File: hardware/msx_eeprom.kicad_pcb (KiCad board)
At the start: 2 copper layers, 102.8 x 65.4 mm, 102 parts, among them J1 Conn_02x07_Odd_Even, P1 MSX_CONNECTOR, U1 AT28C256-15PU

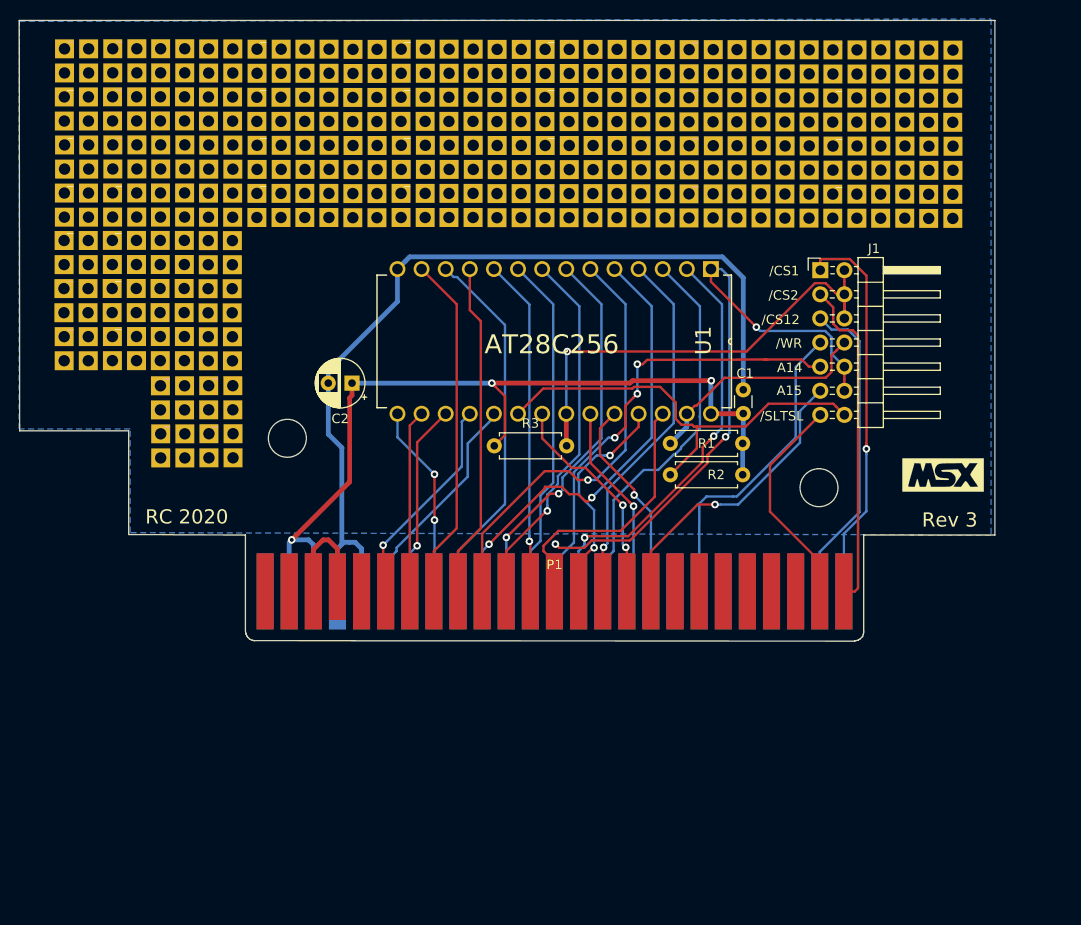
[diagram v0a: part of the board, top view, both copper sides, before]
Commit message: Moved PCB mounting hole up by 1mm
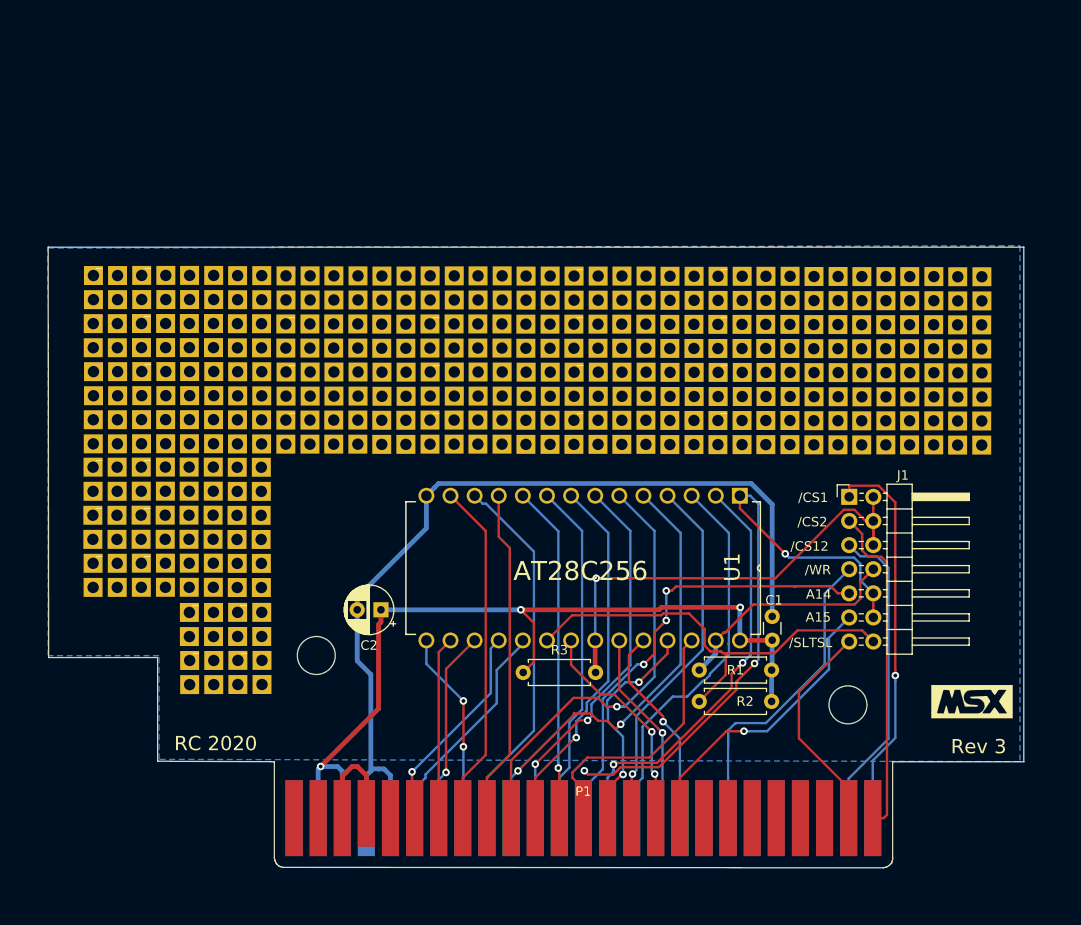
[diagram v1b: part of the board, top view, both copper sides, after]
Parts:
- removed the _ at (96.9, 67.8)
- removed the _ at (96.9, 57.6)
- removed the _ at (86.8, 57.6)
- removed the _ at (96.9, 52.5)
- removed the _ at (91.9, 62.7)
- removed the _ at (102.0, 62.7)
- removed the _ at (96.9, 62.7)
- removed the _ at (86.8, 62.7)
- removed the _ at (117.2, 32.4)
- removed the _ at (157.6, 32.4)
- removed the _ at (127.3, 32.4)
- removed the _ at (102.0, 67.8)
- removed the _ at (172.8, 32.5)
- removed the _ at (132.4, 32.4)
- removed the _ at (107.1, 32.4)
- removed the _ at (122.3, 32.4)
- removed the _ at (91.9, 32.3)
- removed the _ at (167.7, 32.5)
- removed the _ at (102.0, 32.4)
- removed the _ at (112.1, 32.4)
- removed the _ at (142.5, 32.4)
- removed the _ at (177.9, 32.5)
- removed the _ at (102.0, 72.9)
- removed the _ at (162.7, 32.5)
- removed the _ at (137.4, 32.4)
- removed the _ at (147.5, 32.4)
- removed the _ at (96.9, 32.3)
- removed the _ at (122.3, 37.5)
- removed the _ at (86.8, 32.4)
- removed the _ at (152.6, 32.4)
- removed the _ at (132.4, 37.5)
- removed the _ at (127.3, 37.5)
- removed the _ at (172.8, 37.5)
- removed the _ at (96.9, 72.9)
- removed the _ at (91.9, 37.4)
- removed the _ at (102.0, 37.4)
- removed the _ at (112.1, 37.5)
- removed the _ at (107.1, 37.5)
- removed the _ at (117.2, 37.5)
- removed the _ at (167.7, 37.5)
- removed the _ at (177.8, 37.6)
- removed the _ at (142.5, 37.5)
- removed the _ at (157.6, 37.5)
- removed the _ at (152.6, 37.5)
- removed the _ at (91.9, 52.5)
- removed the _ at (162.7, 37.5)
- removed the _ at (137.4, 37.5)
- removed the _ at (147.5, 37.5)
- removed the _ at (86.8, 37.4)
- removed the _ at (96.9, 37.4)
- removed the _ at (122.3, 42.5)
- removed the _ at (132.4, 42.5)
- removed the _ at (127.3, 42.5)
- removed the _ at (172.8, 42.6)
- removed the _ at (91.9, 42.5)
- removed the _ at (102.0, 52.6)
- removed the _ at (102.0, 42.5)
- removed the _ at (112.1, 42.5)
- removed the _ at (107.1, 42.5)
- removed the _ at (117.2, 42.5)
- removed the _ at (167.8, 42.6)
- removed the _ at (177.9, 42.6)
- removed the _ at (142.5, 42.5)
- removed the _ at (157.7, 42.6)
- removed the _ at (152.6, 42.6)
- removed the _ at (162.7, 42.6)
- removed the _ at (101.9, 57.6)
- removed the _ at (137.4, 42.5)
- removed the _ at (147.5, 42.6)
- removed the _ at (86.8, 42.5)
- removed the _ at (96.9, 42.5)
- removed the _ at (86.8, 47.5)
- removed the _ at (96.9, 47.5)
- removed the _ at (91.9, 47.5)
- removed the _ at (102.0, 47.6)
- removed the _ at (112.1, 47.6)
- removed the _ at (107.1, 47.6)
- removed the _ at (91.8, 57.6)
- removed the _ at (117.2, 47.6)
- removed the _ at (172.8, 47.7)
- removed the _ at (167.7, 47.7)
- removed the _ at (177.8, 47.7)
- removed the _ at (157.6, 47.6)
- removed the _ at (152.6, 47.6)
- removed the _ at (162.7, 47.6)
- removed the _ at (137.4, 47.6)
- removed the _ at (147.5, 47.6)
- removed the _ at (142.5, 47.6)
- removed the _ at (86.8, 52.5)
- removed the _ at (132.4, 47.6)
- removed the _ at (127.3, 47.6)
- removed the _ at (122.3, 47.6)
- added _: _, Connector_Wire:SolderWirePad_2x02_P2.54mm_Drill0.8mm, F.Cu at (100.0, 91.7)
- added _: _, Connector_Wire:SolderWirePad_2x02_P2.54mm_Drill0.8mm, F.Cu at (99.9, 81.5)
- added _: _, Connector_Wire:SolderWirePad_2x02_P2.54mm_Drill0.8mm, F.Cu at (89.8, 81.5)
- added _: _, Connector_Wire:SolderWirePad_2x02_P2.54mm_Drill0.8mm, F.Cu at (99.9, 76.4)
- added _: _, Connector_Wire:SolderWirePad_2x02_P2.54mm_Drill0.8mm, F.Cu at (94.9, 86.5)
- added _: _, Connector_Wire:SolderWirePad_2x02_P2.54mm_Drill0.8mm, F.Cu at (105.0, 86.6)
- added _: _, Connector_Wire:SolderWirePad_2x02_P2.54mm_Drill0.8mm, F.Cu at (99.9, 86.5)
- added _: _, Connector_Wire:SolderWirePad_2x02_P2.54mm_Drill0.8mm, F.Cu at (89.8, 86.5)
- added _: _, Connector_Wire:SolderWirePad_2x02_P2.54mm_Drill0.8mm, F.Cu at (120.2, 56.3)
- added _: _, Connector_Wire:SolderWirePad_2x02_P2.54mm_Drill0.8mm, F.Cu at (160.7, 56.3)
- added _: _, Connector_Wire:SolderWirePad_2x02_P2.54mm_Drill0.8mm, F.Cu at (130.4, 56.3)
- added _: _, Connector_Wire:SolderWirePad_2x02_P2.54mm_Drill0.8mm, F.Cu at (105.0, 91.7)
- added _: _, Connector_Wire:SolderWirePad_2x02_P2.54mm_Drill0.8mm, F.Cu at (175.8, 56.3)
- added _: _, Connector_Wire:SolderWirePad_2x02_P2.54mm_Drill0.8mm, F.Cu at (135.4, 56.3)
- added _: _, Connector_Wire:SolderWirePad_2x02_P2.54mm_Drill0.8mm, F.Cu at (110.1, 56.3)
- added _: _, Connector_Wire:SolderWirePad_2x02_P2.54mm_Drill0.8mm, F.Cu at (125.3, 56.3)
- added _: _, Connector_Wire:SolderWirePad_2x02_P2.54mm_Drill0.8mm, F.Cu at (94.9, 56.2)
- added _: _, Connector_Wire:SolderWirePad_2x02_P2.54mm_Drill0.8mm, F.Cu at (170.8, 56.3)
- added _: _, Connector_Wire:SolderWirePad_2x02_P2.54mm_Drill0.8mm, F.Cu at (105.0, 56.2)
- added _: _, Connector_Wire:SolderWirePad_2x02_P2.54mm_Drill0.8mm, F.Cu at (115.2, 56.3)
- added _: _, Connector_Wire:SolderWirePad_2x02_P2.54mm_Drill0.8mm, F.Cu at (145.5, 56.3)
- added _: _, Connector_Wire:SolderWirePad_2x02_P2.54mm_Drill0.8mm, F.Cu at (180.9, 56.4)
- added _: _, Connector_Wire:SolderWirePad_2x02_P2.54mm_Drill0.8mm, F.Cu at (105.1, 96.8)
- added _: _, Connector_Wire:SolderWirePad_2x02_P2.54mm_Drill0.8mm, F.Cu at (165.8, 56.3)
- added _: _, Connector_Wire:SolderWirePad_2x02_P2.54mm_Drill0.8mm, F.Cu at (140.5, 56.3)
- added _: _, Connector_Wire:SolderWirePad_2x02_P2.54mm_Drill0.8mm, F.Cu at (150.6, 56.3)
- added _: _, Connector_Wire:SolderWirePad_2x02_P2.54mm_Drill0.8mm, F.Cu at (100.0, 56.2)
- added _: _, Connector_Wire:SolderWirePad_2x02_P2.54mm_Drill0.8mm, F.Cu at (125.3, 61.3)
- added _: _, Connector_Wire:SolderWirePad_2x02_P2.54mm_Drill0.8mm, F.Cu at (89.9, 56.2)
- added _: _, Connector_Wire:SolderWirePad_2x02_P2.54mm_Drill0.8mm, F.Cu at (155.7, 56.3)
- added _: _, Connector_Wire:SolderWirePad_2x02_P2.54mm_Drill0.8mm, F.Cu at (135.4, 61.4)
- added _: _, Connector_Wire:SolderWirePad_2x02_P2.54mm_Drill0.8mm, F.Cu at (130.3, 61.3)
- added _: _, Connector_Wire:SolderWirePad_2x02_P2.54mm_Drill0.8mm, F.Cu at (175.8, 61.4)
- added _: _, Connector_Wire:SolderWirePad_2x02_P2.54mm_Drill0.8mm, F.Cu at (100.0, 96.8)
- added _: _, Connector_Wire:SolderWirePad_2x02_P2.54mm_Drill0.8mm, F.Cu at (94.9, 61.3)
- added _: _, Connector_Wire:SolderWirePad_2x02_P2.54mm_Drill0.8mm, F.Cu at (105.0, 61.3)
- added _: _, Connector_Wire:SolderWirePad_2x02_P2.54mm_Drill0.8mm, F.Cu at (115.2, 61.3)
- added _: _, Connector_Wire:SolderWirePad_2x02_P2.54mm_Drill0.8mm, F.Cu at (110.1, 61.3)
- added _: _, Connector_Wire:SolderWirePad_2x02_P2.54mm_Drill0.8mm, F.Cu at (120.2, 61.4)
- added _: _, Connector_Wire:SolderWirePad_2x02_P2.54mm_Drill0.8mm, F.Cu at (170.8, 61.4)
- added _: _, Connector_Wire:SolderWirePad_2x02_P2.54mm_Drill0.8mm, F.Cu at (180.9, 61.4)
- added _: _, Connector_Wire:SolderWirePad_2x02_P2.54mm_Drill0.8mm, F.Cu at (145.5, 61.4)
- added _: _, Connector_Wire:SolderWirePad_2x02_P2.54mm_Drill0.8mm, F.Cu at (160.7, 61.4)
- added _: _, Connector_Wire:SolderWirePad_2x02_P2.54mm_Drill0.8mm, F.Cu at (155.6, 61.4)
- added _: _, Connector_Wire:SolderWirePad_2x02_P2.54mm_Drill0.8mm, F.Cu at (94.9, 76.4)
- added _: _, Connector_Wire:SolderWirePad_2x02_P2.54mm_Drill0.8mm, F.Cu at (165.7, 61.4)
- added _: _, Connector_Wire:SolderWirePad_2x02_P2.54mm_Drill0.8mm, F.Cu at (140.5, 61.4)
- added _: _, Connector_Wire:SolderWirePad_2x02_P2.54mm_Drill0.8mm, F.Cu at (150.6, 61.4)
- added _: _, Connector_Wire:SolderWirePad_2x02_P2.54mm_Drill0.8mm, F.Cu at (89.8, 61.3)
- added _: _, Connector_Wire:SolderWirePad_2x02_P2.54mm_Drill0.8mm, F.Cu at (100.0, 61.3)
- added _: _, Connector_Wire:SolderWirePad_2x02_P2.54mm_Drill0.8mm, F.Cu at (125.3, 66.4)
- added _: _, Connector_Wire:SolderWirePad_2x02_P2.54mm_Drill0.8mm, F.Cu at (135.4, 66.4)
- added _: _, Connector_Wire:SolderWirePad_2x02_P2.54mm_Drill0.8mm, F.Cu at (130.4, 66.4)
- added _: _, Connector_Wire:SolderWirePad_2x02_P2.54mm_Drill0.8mm, F.Cu at (175.8, 66.5)
- added _: _, Connector_Wire:SolderWirePad_2x02_P2.54mm_Drill0.8mm, F.Cu at (94.9, 66.3)
- added _: _, Connector_Wire:SolderWirePad_2x02_P2.54mm_Drill0.8mm, F.Cu at (105.0, 76.4)
- added _: _, Connector_Wire:SolderWirePad_2x02_P2.54mm_Drill0.8mm, F.Cu at (105.0, 66.4)
- added _: _, Connector_Wire:SolderWirePad_2x02_P2.54mm_Drill0.8mm, F.Cu at (115.2, 66.4)
- added _: _, Connector_Wire:SolderWirePad_2x02_P2.54mm_Drill0.8mm, F.Cu at (110.1, 66.4)
- added _: _, Connector_Wire:SolderWirePad_2x02_P2.54mm_Drill0.8mm, F.Cu at (120.2, 66.4)
- added _: _, Connector_Wire:SolderWirePad_2x02_P2.54mm_Drill0.8mm, F.Cu at (170.8, 66.5)
- added _: _, Connector_Wire:SolderWirePad_2x02_P2.54mm_Drill0.8mm, F.Cu at (180.9, 66.5)
- added _: _, Connector_Wire:SolderWirePad_2x02_P2.54mm_Drill0.8mm, F.Cu at (145.5, 66.4)
- added _: _, Connector_Wire:SolderWirePad_2x02_P2.54mm_Drill0.8mm, F.Cu at (160.7, 66.4)
- added _: _, Connector_Wire:SolderWirePad_2x02_P2.54mm_Drill0.8mm, F.Cu at (155.7, 66.4)
- added _: _, Connector_Wire:SolderWirePad_2x02_P2.54mm_Drill0.8mm, F.Cu at (165.8, 66.5)
- added _: _, Connector_Wire:SolderWirePad_2x02_P2.54mm_Drill0.8mm, F.Cu at (105.0, 81.5)
- added _: _, Connector_Wire:SolderWirePad_2x02_P2.54mm_Drill0.8mm, F.Cu at (140.5, 66.4)
- added _: _, Connector_Wire:SolderWirePad_2x02_P2.54mm_Drill0.8mm, F.Cu at (150.6, 66.4)
- added _: _, Connector_Wire:SolderWirePad_2x02_P2.54mm_Drill0.8mm, F.Cu at (89.9, 66.4)
- added _: _, Connector_Wire:SolderWirePad_2x02_P2.54mm_Drill0.8mm, F.Cu at (100.0, 66.3)
- added _: _, Connector_Wire:SolderWirePad_2x02_P2.54mm_Drill0.8mm, F.Cu at (89.8, 71.4)
- added _: _, Connector_Wire:SolderWirePad_2x02_P2.54mm_Drill0.8mm, F.Cu at (100.0, 71.4)
- added _: _, Connector_Wire:SolderWirePad_2x02_P2.54mm_Drill0.8mm, F.Cu at (94.9, 71.4)
- added _: _, Connector_Wire:SolderWirePad_2x02_P2.54mm_Drill0.8mm, F.Cu at (105.0, 71.4)
- added _: _, Connector_Wire:SolderWirePad_2x02_P2.54mm_Drill0.8mm, F.Cu at (115.2, 71.5)
- added _: _, Connector_Wire:SolderWirePad_2x02_P2.54mm_Drill0.8mm, F.Cu at (110.1, 71.5)
- added _: _, Connector_Wire:SolderWirePad_2x02_P2.54mm_Drill0.8mm, F.Cu at (94.9, 81.5)
- added _: _, Connector_Wire:SolderWirePad_2x02_P2.54mm_Drill0.8mm, F.Cu at (120.2, 71.5)
- added _: _, Connector_Wire:SolderWirePad_2x02_P2.54mm_Drill0.8mm, F.Cu at (175.8, 71.5)
- added _: _, Connector_Wire:SolderWirePad_2x02_P2.54mm_Drill0.8mm, F.Cu at (170.8, 71.5)
- added _: _, Connector_Wire:SolderWirePad_2x02_P2.54mm_Drill0.8mm, F.Cu at (180.9, 71.6)
- added _: _, Connector_Wire:SolderWirePad_2x02_P2.54mm_Drill0.8mm, F.Cu at (160.7, 71.5)
- added _: _, Connector_Wire:SolderWirePad_2x02_P2.54mm_Drill0.8mm, F.Cu at (155.6, 71.5)
- added _: _, Connector_Wire:SolderWirePad_2x02_P2.54mm_Drill0.8mm, F.Cu at (165.7, 71.5)
- added _: _, Connector_Wire:SolderWirePad_2x02_P2.54mm_Drill0.8mm, F.Cu at (140.5, 71.5)
- added _: _, Connector_Wire:SolderWirePad_2x02_P2.54mm_Drill0.8mm, F.Cu at (150.6, 71.5)
- added _: _, Connector_Wire:SolderWirePad_2x02_P2.54mm_Drill0.8mm, F.Cu at (145.5, 71.5)
- added _: _, Connector_Wire:SolderWirePad_2x02_P2.54mm_Drill0.8mm, F.Cu at (89.8, 76.4)
- added _: _, Connector_Wire:SolderWirePad_2x02_P2.54mm_Drill0.8mm, F.Cu at (135.4, 71.5)
- added _: _, Connector_Wire:SolderWirePad_2x02_P2.54mm_Drill0.8mm, F.Cu at (130.4, 71.5)
- added _: _, Connector_Wire:SolderWirePad_2x02_P2.54mm_Drill0.8mm, F.Cu at (125.3, 71.5)
- moved C1 24.1 mm to (161.4, 94.6)
- moved C2 24.1 mm to (120.1, 91.4)
- moved G*** 24.1 mm to (182.4, 101.1)
- moved J1 24.1 mm to (169.5, 79.5)
- moved P1 24.1 mm to (140.2, 110.2)
- moved R1 24.1 mm to (161.3, 97.8)
- moved R2 24.1 mm to (161.3, 101.1)
- moved U1 24.1 mm to (124.9, 94.7)
- moved G*** 24.1 mm to (142.7, 86.9)
- moved R3 24.1 mm to (135.1, 98.0)

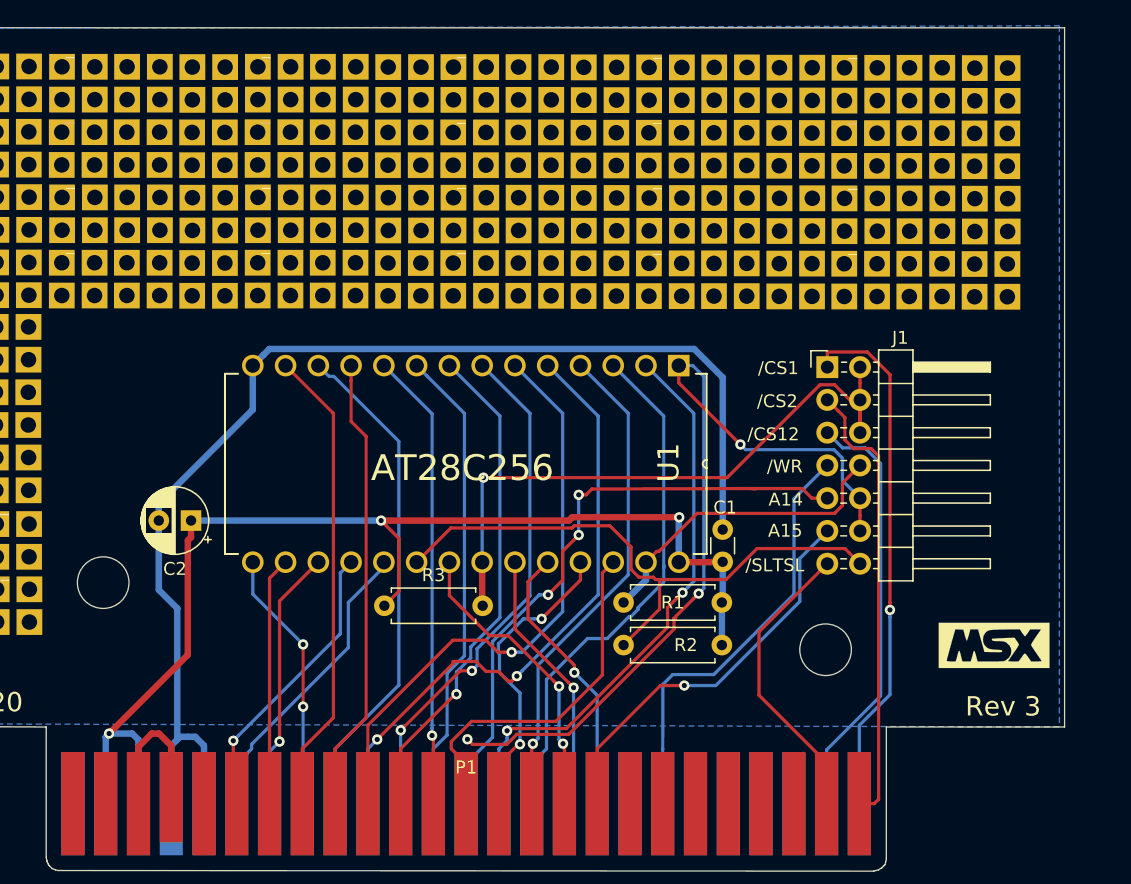
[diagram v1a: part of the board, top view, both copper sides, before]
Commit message: Moved jumpers to a position for easier access when connected to MSX
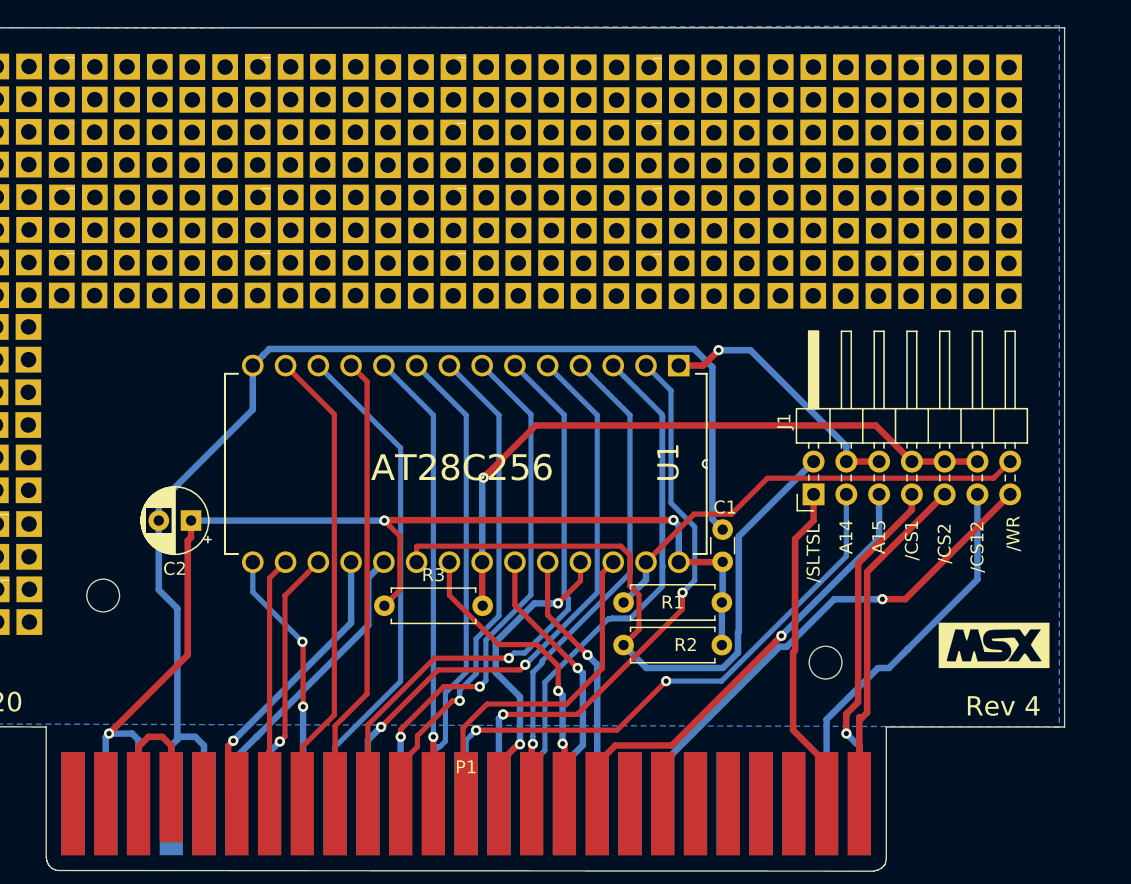
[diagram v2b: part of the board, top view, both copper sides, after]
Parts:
- removed the _ at (175.8, 56.3)
- removed the _ at (170.8, 56.3)
- removed the _ at (180.9, 56.4)
- removed the _ at (165.8, 56.3)
- removed the _ at (175.8, 61.4)
- removed the _ at (170.8, 61.4)
- removed the _ at (180.9, 61.4)
- removed the _ at (165.7, 61.4)
- removed the _ at (175.8, 66.5)
- removed the _ at (170.8, 66.5)
- removed the _ at (180.9, 66.5)
- removed the _ at (165.8, 66.5)
- removed the _ at (175.8, 71.5)
- removed the _ at (170.8, 71.5)
- removed the _ at (180.9, 71.6)
- removed the _ at (165.7, 71.5)
- added _: _, Connector_Wire:SolderWirePad_2x02_P2.54mm_Drill0.8mm, F.Cu at (170.9, 71.5)
- added _: _, Connector_Wire:SolderWirePad_2x02_P2.54mm_Drill0.8mm, F.Cu at (165.9, 66.4)
- added _: _, Connector_Wire:SolderWirePad_2x02_P2.54mm_Drill0.8mm, F.Cu at (181.0, 66.4)
- added _: _, Connector_Wire:SolderWirePad_2x02_P2.54mm_Drill0.8mm, F.Cu at (176.0, 61.4)
- added _: _, Connector_Wire:SolderWirePad_2x02_P2.54mm_Drill0.8mm, F.Cu at (170.9, 61.4)
- added _: _, Connector_Wire:SolderWirePad_2x02_P2.54mm_Drill0.8mm, F.Cu at (181.0, 61.4)
- added _: _, Connector_Wire:SolderWirePad_2x02_P2.54mm_Drill0.8mm, F.Cu at (176.0, 56.3)
- added _: _, Connector_Wire:SolderWirePad_2x02_P2.54mm_Drill0.8mm, F.Cu at (165.8, 61.4)
- added _: _, Connector_Wire:SolderWirePad_2x02_P2.54mm_Drill0.8mm, F.Cu at (170.9, 66.4)
- added _: _, Connector_Wire:SolderWirePad_2x02_P2.54mm_Drill0.8mm, F.Cu at (176.0, 71.5)
- added _: _, Connector_Wire:SolderWirePad_2x02_P2.54mm_Drill0.8mm, F.Cu at (181.0, 71.5)
- added _: _, Connector_Wire:SolderWirePad_2x02_P2.54mm_Drill0.8mm, F.Cu at (170.9, 56.3)
- added _: _, Connector_Wire:SolderWirePad_2x02_P2.54mm_Drill0.8mm, F.Cu at (165.8, 56.3)
- added _: _, Connector_Wire:SolderWirePad_2x02_P2.54mm_Drill0.8mm, F.Cu at (181.0, 56.3)
- added _: _, Connector_Wire:SolderWirePad_2x02_P2.54mm_Drill0.8mm, F.Cu at (165.8, 71.5)
- added _: _, Connector_Wire:SolderWirePad_2x02_P2.54mm_Drill0.8mm, F.Cu at (176.0, 66.4)
- moved J1 9.92 mm to (168.4, 89.4), turned to 90 degrees
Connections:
- J1 pad 1: cs1 -> sltsl
- J1 pad 10: mem_A14 -> mem_oe
- J1 pad 11: A15 -> cs12
- J1 pad 12: mem_A14 -> mem_oe
- J1 pad 13: sltsl -> wr
- J1 pad 14: mem_ce -> mem_we
- J1 pad 2: mem_oe -> mem_ce
- J1 pad 3: cs2 -> A14
- J1 pad 4: mem_oe -> mem_A14
- J1 pad 5: cs12 -> A15
- J1 pad 6: mem_oe -> mem_A14
- J1 pad 7: wr -> cs1
- J1 pad 8: mem_we -> mem_oe
- J1 pad 9: A14 -> cs2
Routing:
- net mem_A14: track 65.6 -> 20.3 mm, vias 3 -> 1
- net A7: track 41.0 -> 64.7 mm
- net cs1: track 41.0 -> 27.4 mm
- net mem_we: track 24.6 -> 35.3 mm
- net cs2: track 35.7 -> 27.0 mm
- net A15: track 31.0 -> 38.8 mm
- net mem_ce: track 46.0 -> 53.1 mm
- net wr: track 33.4 -> 38.7 mm, vias 0 -> 1
- net A1: track 36.5 -> 41.5 mm
- net cs12: track 33.2 -> 30.3 mm
- net sltsl: track 26.1 -> 28.9 mm
- net mem_oe: track 49.8 -> 51.7 mm
- net A9: track 21.6 -> 20.3 mm
- net A3: track 40.2 -> 41.4 mm
- net A5: track 47.8 -> 46.6 mm
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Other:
- board text added: "Rev 4"
- board text removed: "Rev 3"
